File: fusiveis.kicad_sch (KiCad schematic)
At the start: 20 parts, among them J4 DC_CONVERTER, J5 VBAT

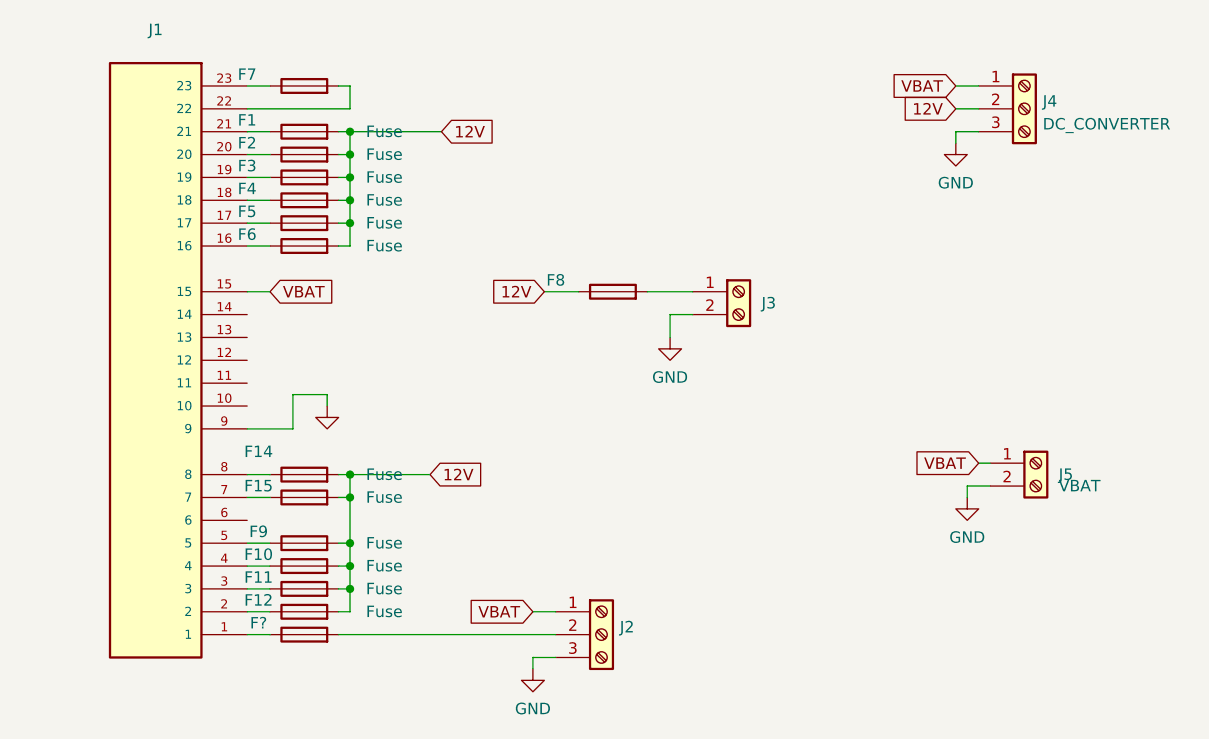
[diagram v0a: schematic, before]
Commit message: MOD: placa de fusiveis nova
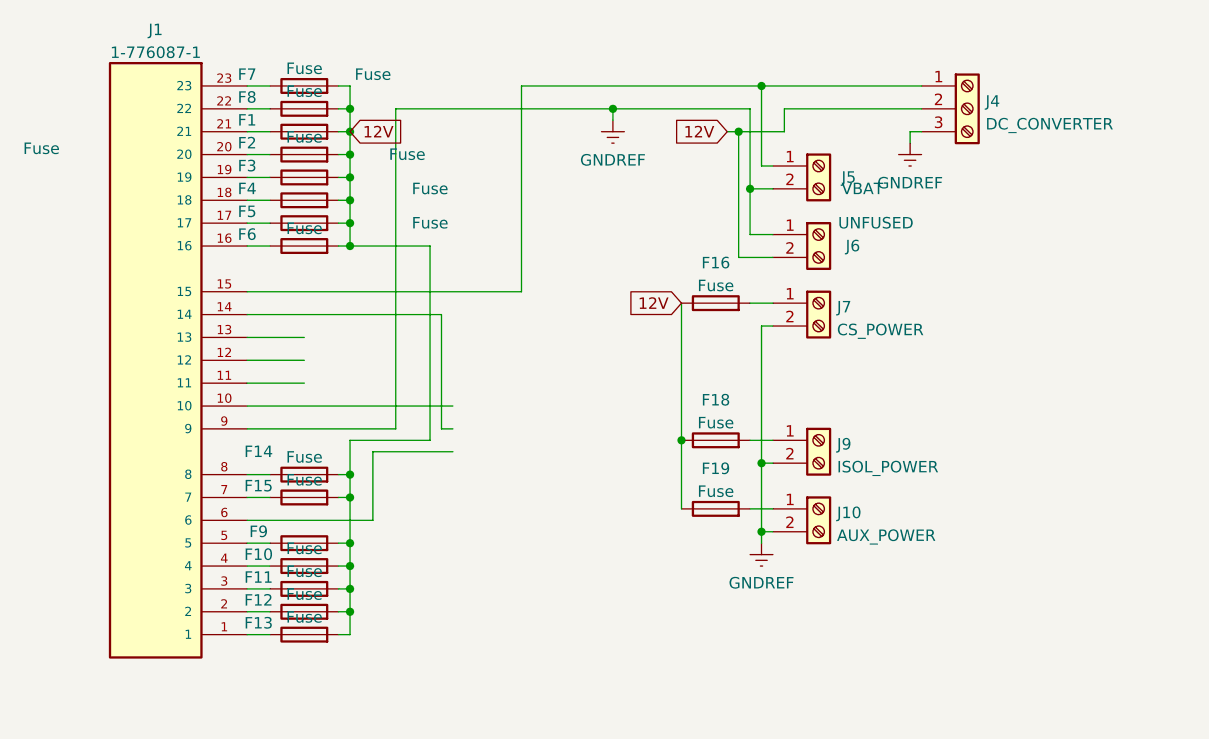
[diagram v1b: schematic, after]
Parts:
- removed F?: (no value), symbol Device:Fuse
- removed J2: (no value), symbol Connector:Screw_Terminal_01x03
- removed J3: (no value), symbol Connector:Screw_Terminal_01x02
- added F13, F16, F18, F19: Fuse, Fuse:Fuseholder_Cylinder-5x20mm_Schurter_0031_8201_Horizontal_Open, symbol Device:Fuse
- added J10: AUX_POWER, TerminalBlock:TerminalBlock_bornier-2_P5.08mm, symbol Connector:Screw_Terminal_01x02
- added J6: UNFUSED, TerminalBlock:TerminalBlock_bornier-2_P5.08mm, symbol Connector:Screw_Terminal_01x02
- added J7: CS_POWER, TerminalBlock:TerminalBlock_bornier-2_P5.08mm, symbol Connector:Screw_Terminal_01x02
- added J9: ISOL_POWER, TerminalBlock:TerminalBlock_bornier-2_P5.08mm, symbol Connector:Screw_Terminal_01x02
- F7, F8: value (none) -> Fuse; footprint (none) -> Fuse:Fuseholder_Cylinder-5x20mm_Schurter_0031_8201_Horizontal_Open
- J1: value (none) -> 1-776087-1; footprint (none) -> Ampseal 23:TE_1-776087-1
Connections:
- net 12V: now also F7.2, F8.2, F13.2, F16.1, F18.1, F19.1, J6.2 (Pin_2); no longer F8.1
- net at J1.1: now also F13.1
- net at J1.22: now also F8.1; no longer F7.2
- net GND renamed GNDREF
- net GNDREF: now also J10.2 (Pin_2), J6.1 (Pin_1), J7.2 (Pin_2), J9.2 (Pin_2)
- net VBAT: no longer names the net of J1.15, J4.1 (Pin_1), J5.1 (Pin_1)
- new net: F19.2, J10.1 (Pin_1)
- new net: F16.2, J7.1 (Pin_1)
- new net: F18.2, J9.1 (Pin_1)
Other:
- moved on the sheet: J4, J5
